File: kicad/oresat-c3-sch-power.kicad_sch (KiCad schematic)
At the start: 58 parts, among them U31 LP2985AIM5-3.3, U34 TPS259621DDA, U35 TPS259620DDA, U36 LTC3624-5, U38 LP2985AIM5-3.3, U6 LTC3624-5

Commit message: Fixed test points; added RF test points. Started on layout and component packages for UHF radio.
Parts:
- TP10, TP11, TP14, TP15, TP16: footprint TestPoint:TestPoint_Pad_D1.0mm -> oresat-misc:TestPoint_Pad_D1.0mm
- TP110, TP12, TP13, TP151, TP17, TP18, TP2: footprint TestPoint:TestPoint_Pad_D1.0mm -> oresat-misc:TestPoint-0.75mm-th
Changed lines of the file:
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@@
       (effects (font (size 1.27 1.27)) hide)
     )
-    (property "Footprint" "TestPoint:TestPoint_Pad_D1.0mm" (at 337.82 140.97 0)
+    (property "Footprint" "oresat-misc:TestPoint-0.75mm-th" (at 337.82 140.97 0)
       (effects (font (size 1.27 1.27)) hide)
     )
@@
       (effects (font (size 1.27 1.27)) hide)
     )
-    (property "Footprint" "TestPoint:TestPoint_Pad_D1.0mm" (at 134.62 146.05 0)
+    (property "Footprint" "oresat-misc:TestPoint_Pad_D1.0mm" (at 134.62 146.05 0)
       (effects (font (size 1.27 1.27)) hide)
     )
@@
       (effects (font (size 1.27 1.27)) hide)
     )
-    (property "Footprint" "TestPoint:TestPoint_Pad_D1.0mm" (at 134.62 148.59 0)
+    (property "Footprint" "oresat-misc:TestPoint_Pad_D1.0mm" (at 134.62 148.59 0)
       (effects (font (size 1.27 1.27)) hide)
     )
@@
       (effects (font (size 1.27 1.27)) hide)
     )
-    (property "Footprint" "TestPoint:TestPoint_Pad_D1.0mm" (at 201.93 67.31 0)
+    (property "Footprint" "oresat-misc:TestPoint_Pad_D1.0mm" (at 201.93 67.31 0)
       (effects (font (size 1.27 1.27)) hide)
     )
@@
       (effects (font (size 1.27 1.27)) hide)
     )
-    (property "Footprint" "TestPoint:TestPoint_Pad_D1.0mm" (at 337.82 175.26 0)
+    (property "Footprint" "oresat-misc:TestPoint-0.75mm-th" (at 337.82 175.26 0)
       (effects (font (size 1.27 1.27)) hide)
     )
@@
       (effects (font (size 1.27 1.27)) hide)
     )
-    (property "Footprint" "TestPoint:TestPoint_Pad_D1.0mm" (at 306.07 62.23 0)
+    (property "Footprint" "oresat-misc:TestPoint-0.75mm-th" (at 306.07 62.23 0)
       (effects (font (size 1.27 1.27)) hide)
     )
@@
       (effects (font (size 1.27 1.27)) hide)
     )
-    (property "Footprint" "TestPoint:TestPoint_Pad_D1.0mm" (at 110.49 156.21 0)
+    (property "Footprint" "oresat-misc:TestPoint_Pad_D1.0mm" (at 110.49 156.21 0)
       (effects (font (size 1.27 1.27)) hide)
     )
@@
       (effects (font (size 1.27 1.27)) hide)
     )
-    (property "Footprint" "TestPoint:TestPoint_Pad_D1.0mm" (at 204.47 62.23 0)
+    (property "Footprint" "oresat-misc:TestPoint-0.75mm-th" (at 204.47 62.23 0)
       (effects (font (size 1.27 1.27)) hide)
     )
@@
       (effects (font (size 1.27 1.27)) hide)
     )
-    (property "Footprint" "TestPoint:TestPoint_Pad_D1.0mm" (at 147.32 82.55 0)
+    (property "Footprint" "oresat-misc:TestPoint-0.75mm-th" (at 147.32 82.55 0)
       (effects (font (size 1.27 1.27)) hide)
     )
@@
       (effects (font (size 1.27 1.27)) hide)
     )
-    (property "Footprint" "TestPoint:TestPoint_Pad_D1.0mm" (at 201.93 69.85 0)
+    (property "Footprint" "oresat-misc:TestPoint_Pad_D1.0mm" (at 201.93 69.85 0)
       (effects (font (size 1.27 1.27)) hide)
     )
@@
       (effects (font (size 1.27 1.27)) hide)
     )
-    (property "Footprint" "TestPoint:TestPoint_Pad_D1.0mm" (at 261.62 140.97 0)
+    (property "Footprint" "oresat-misc:TestPoint-0.75mm-th" (at 261.62 140.97 0)
       (effects (font (size 1.27 1.27)) hide)
     )
@@
       (effects (font (size 1.27 1.27)) hide)
     )
-    (property "Footprint" "TestPoint:TestPoint_Pad_D1.0mm" (at 134.62 140.97 0)
-      (effects (font (size 1.27 1.27)) hide)
-    )
+    (property "Footprint" "oresat-misc:TestPoint-0.75mm-th" (at 134.62 140.97 0)
+      (effects (font (size 1.27 1.27)) hide)
+    )

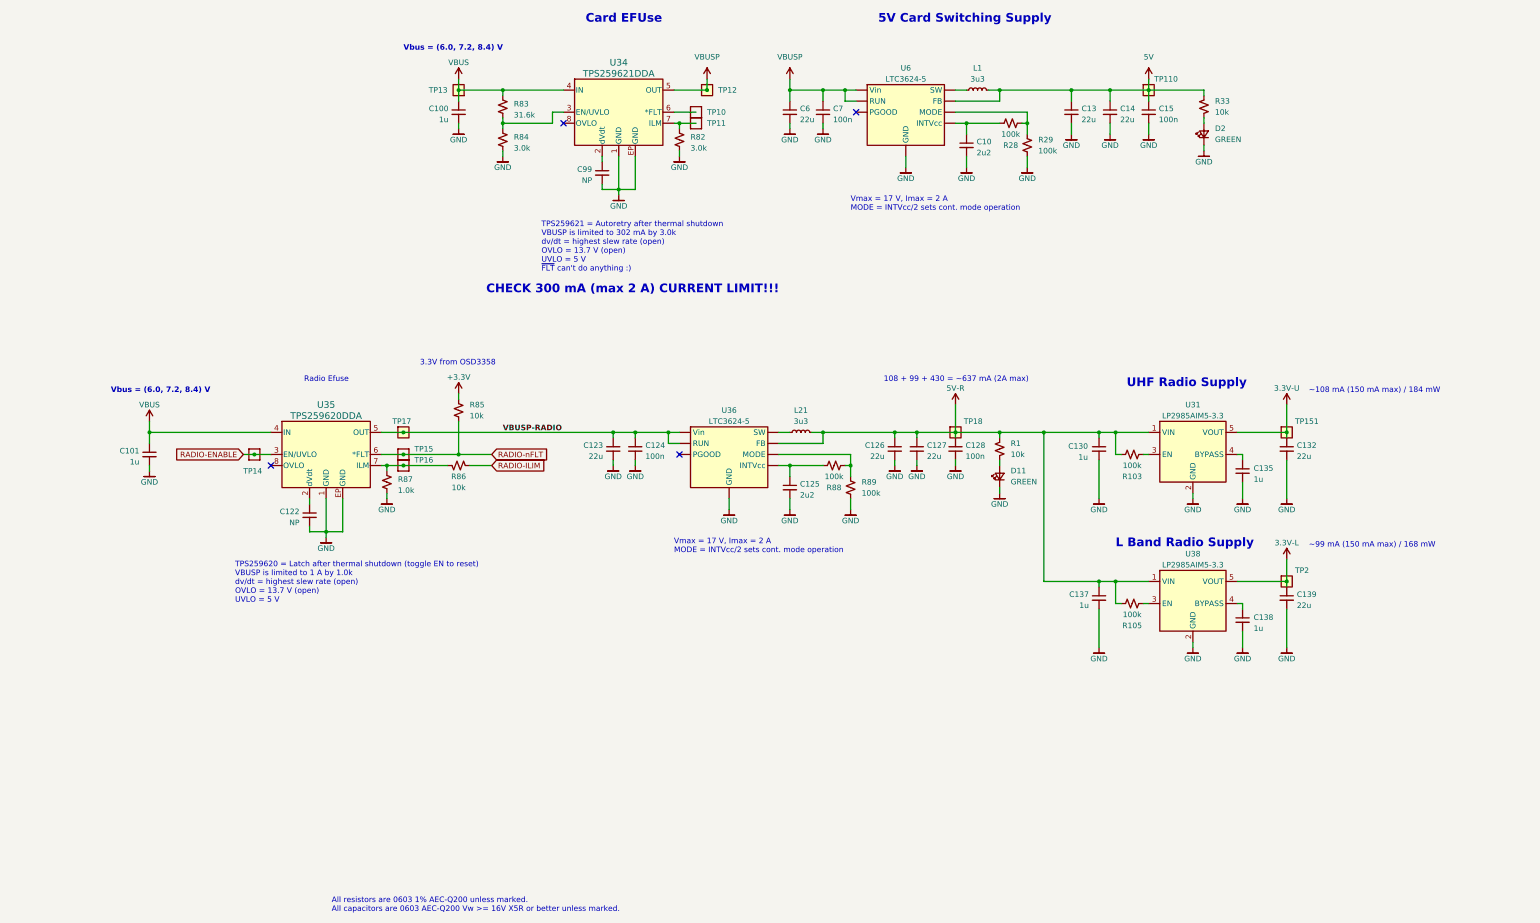
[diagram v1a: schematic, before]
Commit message: Fixed footprints and laid out WDT and OPD circuitry.
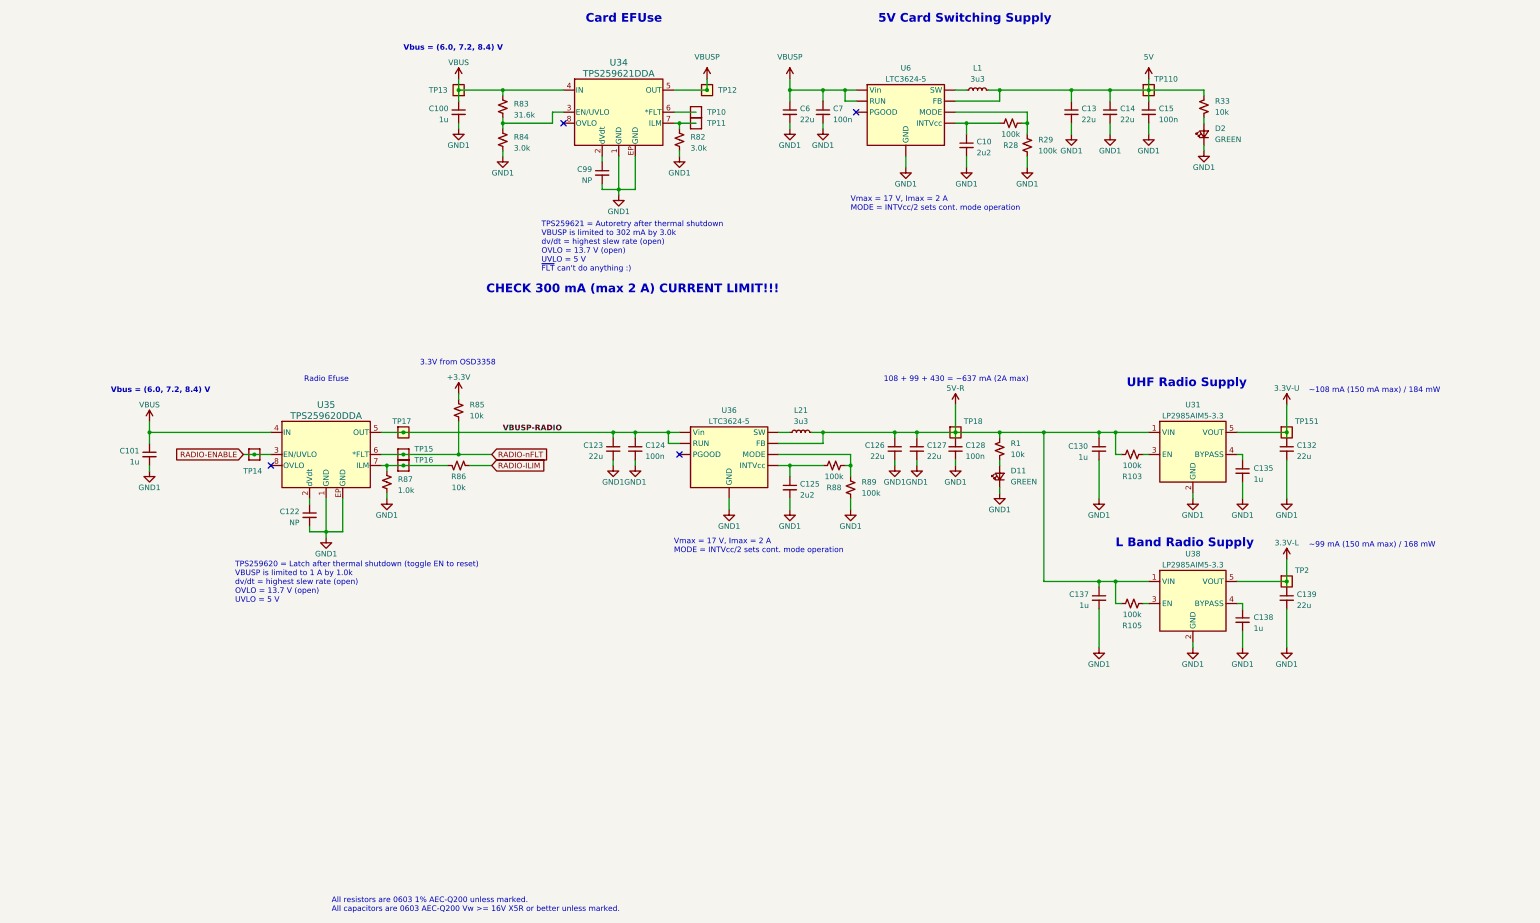
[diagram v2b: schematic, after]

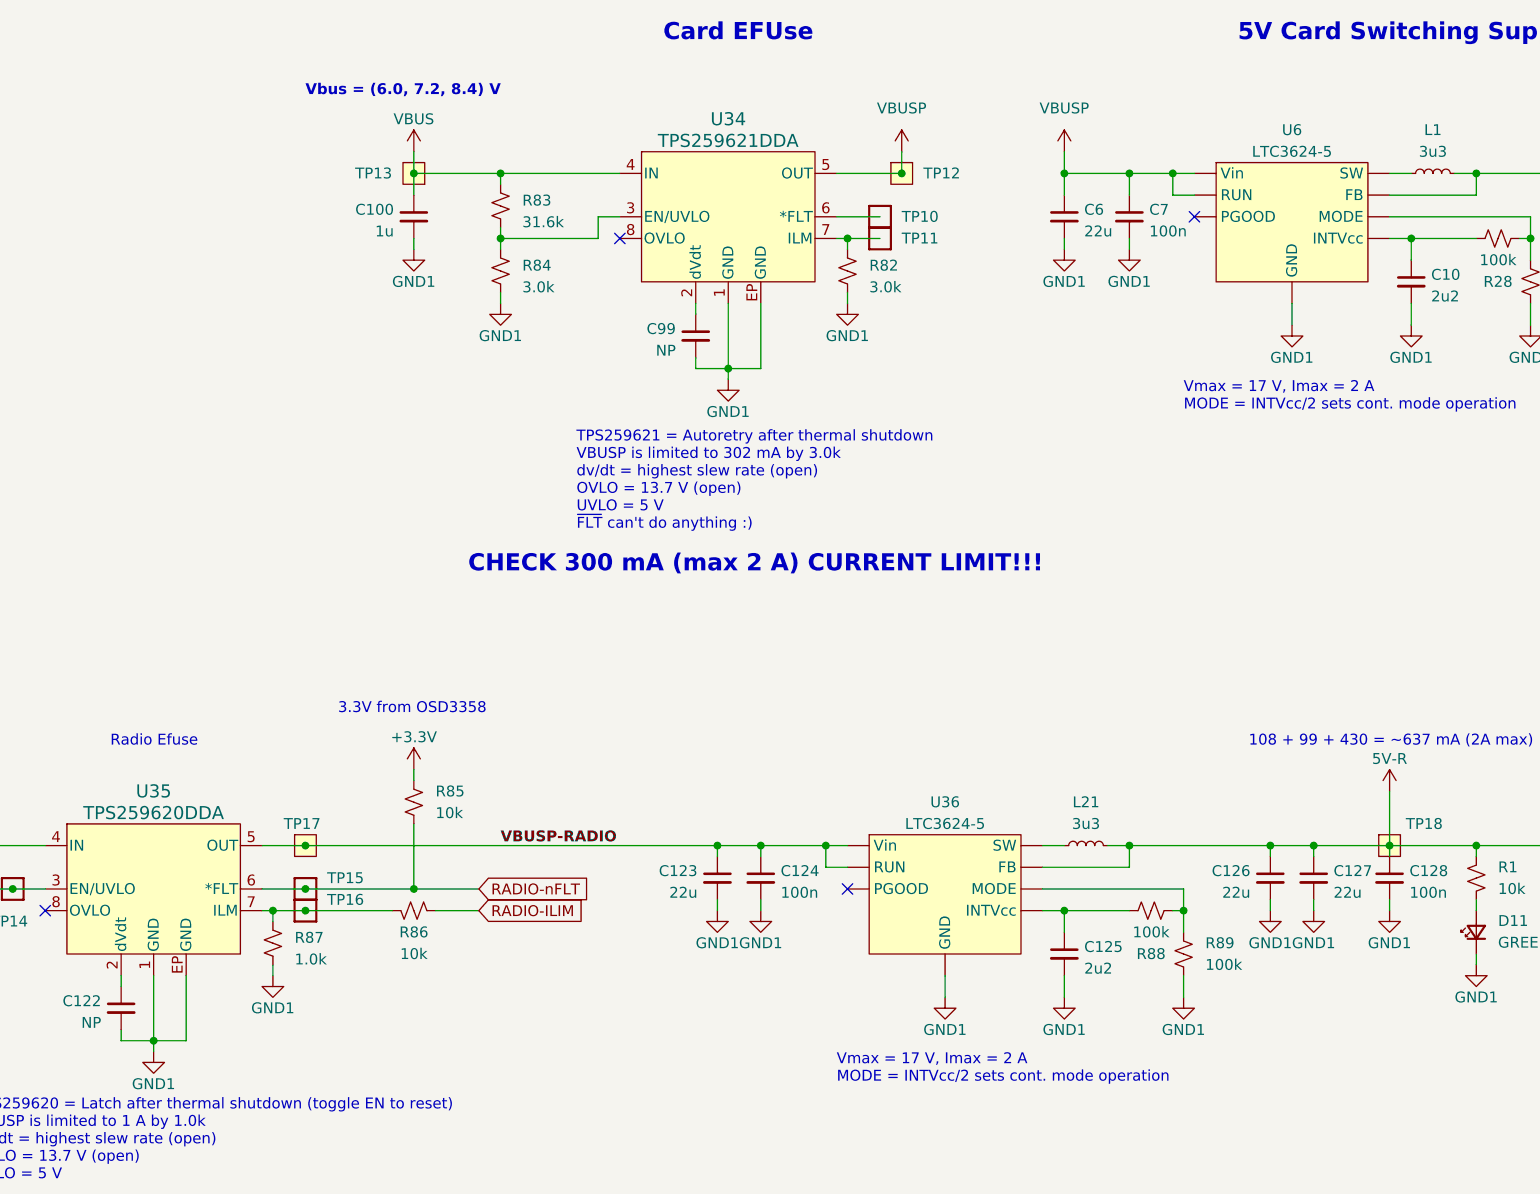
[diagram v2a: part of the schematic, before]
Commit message: More progress on C3 v6. All ICs and Packages are in, deployer and power supply and I2C subsystems laid out.
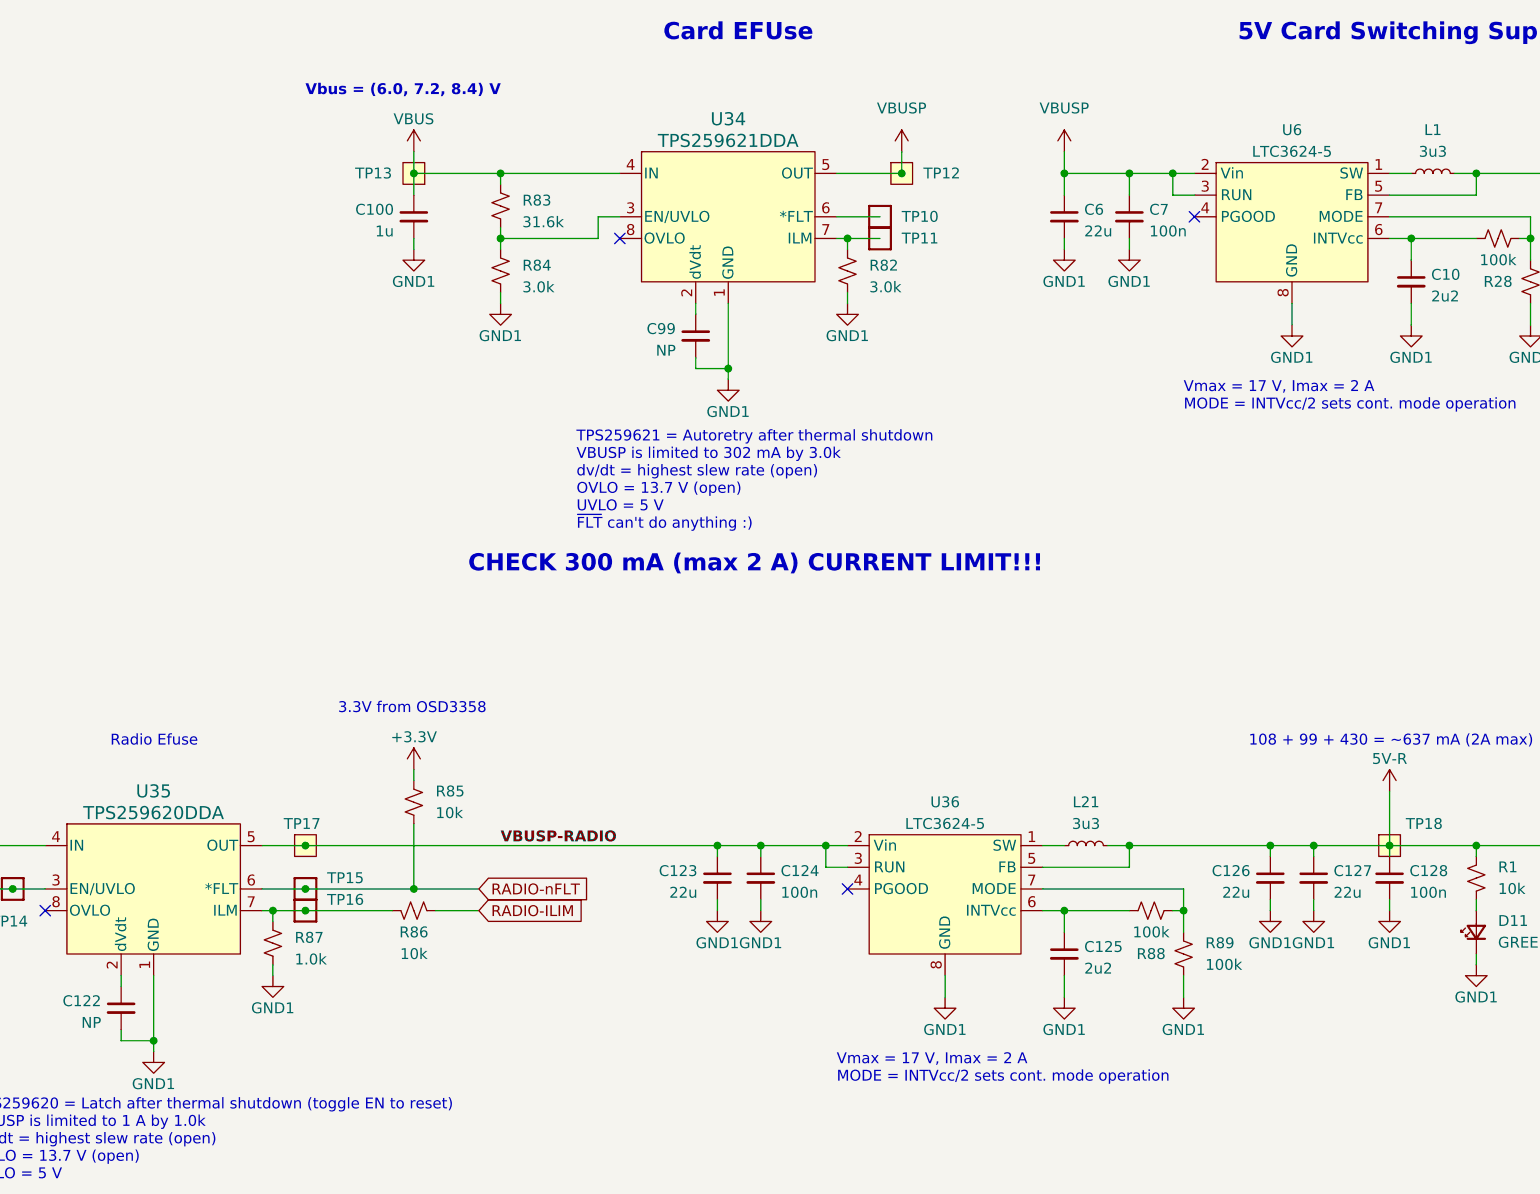
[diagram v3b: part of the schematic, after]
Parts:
- L21: footprint oresat-footprints:L_ECS-MPI4040 -> oresat-passives:L_ECS-MPI4040
- U34, U35: footprint Package_SO:Texas_R-PDSO-G8_EP2.95x4.9mm_Mask2.4x3.1mm -> Package_SO:Texas_R-PDSO-G8_EP2.95x4.9mm_Mask2.4x3.1mm_ThermalVias
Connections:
- net GND: now also U34.9 (GND), U35.9 (GND); no longer U34.EP (GND), U35.EP (GND)
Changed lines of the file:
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@@
   (junction (at 231.14 72.39) (diameter 0) (color 0 0 0 0)
   )
-  (junction (at 184.15 95.25) (diameter 0) (color 0 0 0 0)
-  )
   (junction (at 157.48 80.01) (diameter 0) (color 0 0 0 0)
   )
@@
   (junction (at 76.2 151.13) (diameter 0) (color 0 0 0 0)
   )
+  (junction (at 184.15 95.25) (diameter 0) (color 0 0 0 0)
+  )
   (junction (at 100.33 156.21) (diameter 0) (color 0 0 0 0)
   )
@@
     (stroke (width 0) (type default))
   )
-  (wire (pts (xy 120.65 173.99) (xy 116.84 173.99))
+  (wire (pts (xy 184.15 87.63) (xy 184.15 95.25))
     (stroke (width 0) (type default))
   )
@@
     (stroke (width 0) (type default))
   )
-  (wire (pts (xy 187.96 87.63) (xy 187.96 95.25))
-    (stroke (width 0) (type default))
-  )
   (wire (pts (xy 187.96 151.13) (xy 187.96 152.4))
     (stroke (width 0) (type default))
@@
     (stroke (width 0) (type default))
   )
-  (wire (pts (xy 184.15 87.63) (xy 184.15 95.25))
-    (stroke (width 0) (type default))
-  )
   (wire (pts (xy 288.29 72.39) (xy 297.18 72.39))
     (stroke (width 0) (type default))
@@
     (stroke (width 0) (type default))
   )
-  (wire (pts (xy 187.96 95.25) (xy 184.15 95.25))
-    (stroke (width 0) (type default))
-  )
   (wire (pts (xy 147.32 156.21) (xy 134.62 156.21))
     (stroke (width 0) (type default))
@@
     (stroke (width 0) (type default))
   )
-  (wire (pts (xy 120.65 166.37) (xy 120.65 173.99))
-    (stroke (width 0) (type default))
-  )
   (wire (pts (xy 264.16 87.63) (xy 264.16 90.17))
     (stroke (width 0) (type default))
@@
       (effects (font (size 1.27 1.27)))
     )
-    (property "Footprint" "oresat-footprints:L_ECS-MPI4040" (at 226.06 151.13 0)
+    (property "Footprint" "oresat-passives:L_ECS-MPI4040" (at 226.06 151.13 0)
       (effects (font (size 1.27 1.27)) hide)
     )
@@
       (effects (font (size 1.524 1.524)))
     )
-    (property "Footprint" "Package_SO:Texas_R-PDSO-G8_EP2.95x4.9mm_Mask2.4x3.1mm" (at 184.15 60.96 0)
+    (property "Footprint" "Package_SO:Texas_R-PDSO-G8_EP2.95x4.9mm_Mask2.4x3.1mm_ThermalVias" (at 184.15 60.96 0)
       (effects (font (size 1.27 1.27) italic) hide)
     )
@@
     (pin "7")
     (pin "8")
-    (pin "EP")
+    (pin "9")
     (instances
       (project "oresat-c3"
@@
       (effects (font (size 1.524 1.524)))
     )
-    (property "Footprint" "Package_SO:Texas_R-PDSO-G8_EP2.95x4.9mm_Mask2.4x3.1mm" (at 116.84 139.7 0)
+    (property "Footprint" "Package_SO:Texas_R-PDSO-G8_EP2.95x4.9mm_Mask2.4x3.1mm_ThermalVias" (at 116.84 139.7 0)
       (effects (font (size 1.27 1.27) italic) hide)
     )
@@
     (pin "7")
     (pin "8")
-    (pin "EP")
+    (pin "9")
     (instances
       (project "oresat-c3"
